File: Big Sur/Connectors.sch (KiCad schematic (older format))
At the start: 11 parts, among them J1 XT30, J10 XT30, J11 XT30, J2 XT30, J3 XT30, J4 XT30, J5 XT30, J6 SMD CASTELLATION PKG, J7 XT30, J8 XT30, J9 XT30

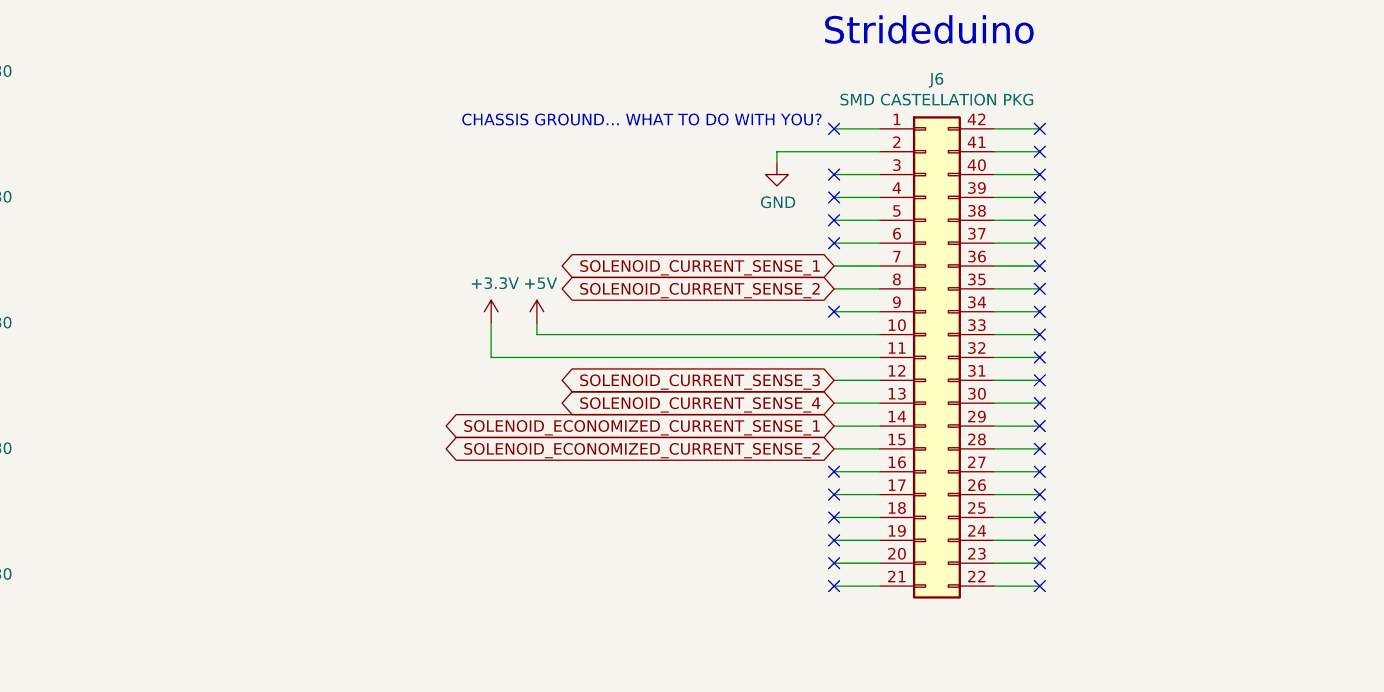
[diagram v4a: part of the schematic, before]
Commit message: Schematics Complete
Still need to spec resistors, and XT30s, then should be ready for layout and routing.
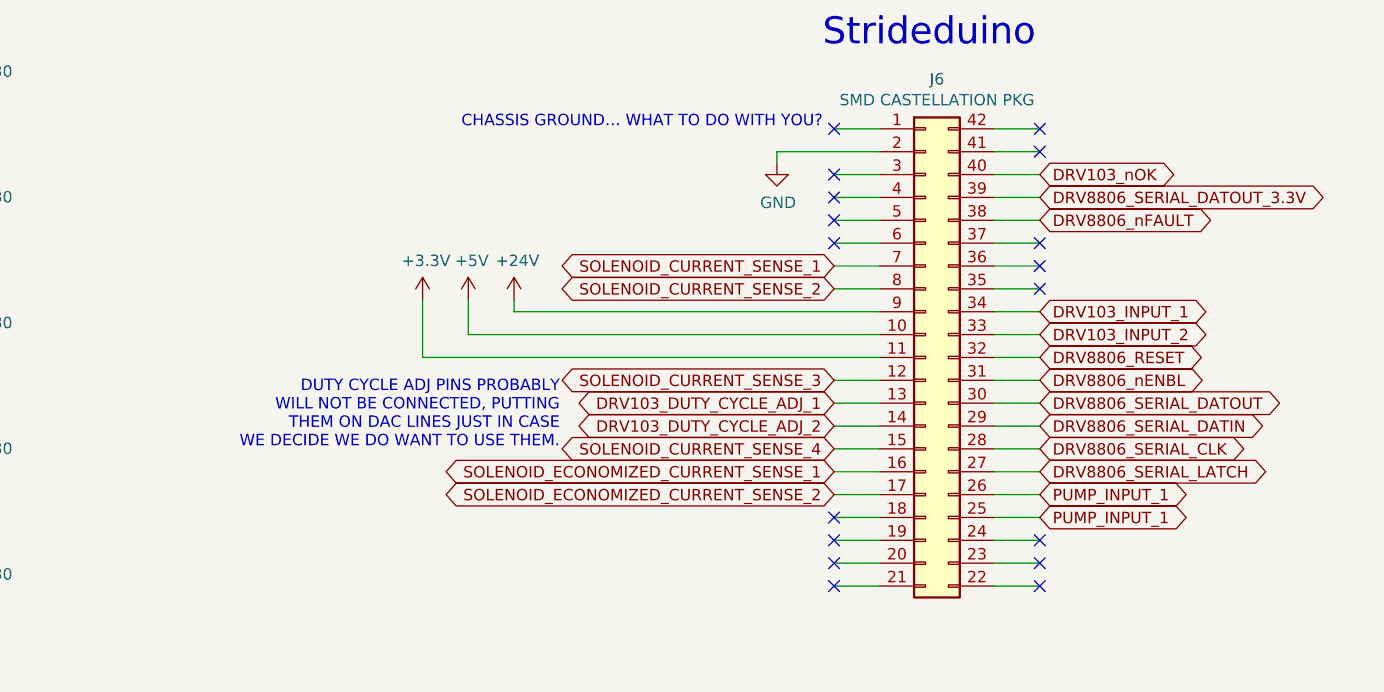
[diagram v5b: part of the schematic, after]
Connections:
- net +24V: now also J6.9 (Pin_9)
- net SOLENOID_CURRENT_SENSE_4: now also J6.15 (Pin_15); no longer J6.13 (Pin_13)
- net SOLENOID_ECONOMIZED_CURRENT_SENSE_1: now also J6.16 (Pin_16); no longer J6.14 (Pin_14)
- net SOLENOID_ECONOMIZED_CURRENT_SENSE_2: now also J6.17 (Pin_17); no longer J6.15 (Pin_15)
- net PUMP_INPUT_1: now reaches J6.25 (Pin_25)
- net PUMP_INPUT_1: now also J6.26 (Pin_26)
- net DRV8806_SERIAL_LATCH: now reaches J6.27 (Pin_27)
- net DRV8806_SERIAL_CLK: now reaches J6.28 (Pin_28)
- net DRV8806_SERIAL_DATIN: now reaches J6.29 (Pin_29)
- net DRV8806_SERIAL_DATOUT: now reaches J6.30 (Pin_30)
- net DRV8806_nENBL: now reaches J6.31 (Pin_31)
- net DRV8806_RESET: now reaches J6.32 (Pin_32)
- net DRV103_INPUT_2: now reaches J6.33 (Pin_33)
- net DRV103_INPUT_1: now reaches J6.34 (Pin_34)
- net DRV8806_nFAULT: now reaches J6.38 (Pin_38)
- net DRV8806_SERIAL_DATOUT_3.3V: now reaches J6.39 (Pin_39)
- net DRV103_nOK: now reaches J6.40 (Pin_40)
- new net DRV103_DUTY_CYCLE_ADJ_1: J6.13 (Pin_13)
- new net DRV103_DUTY_CYCLE_ADJ_2: J6.14 (Pin_14)
- no-connect marks 33 -> 17
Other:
- note added: "DUTY CYCLE ADJ PINS PROBABLY\nWILL NOT BE CONNECTED, PUTTING\nTHEM ON DAC LINES JUST IN CASE\nWE DECIDE WE DO WANT TO USE THEM."
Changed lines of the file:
@@
 NoConn ~ 9650 2150
 NoConn ~ 9650 2250
-NoConn ~ 9650 2350
-NoConn ~ 9650 2450
-NoConn ~ 9650 2550
 NoConn ~ 9650 2650
 NoConn ~ 9650 2750
 NoConn ~ 9650 2850
-NoConn ~ 9650 2950
-NoConn ~ 9650 3050
-NoConn ~ 9650 3150
-NoConn ~ 9650 3250
-NoConn ~ 9650 3350
-NoConn ~ 9650 3450
-NoConn ~ 9650 3550
-NoConn ~ 9650 3650
-NoConn ~ 9650 3750
-NoConn ~ 9650 3850
 NoConn ~ 9650 3950
 NoConn ~ 9650 4050
@@
 NoConn ~ 8750 3950
 NoConn ~ 8750 3850
-NoConn ~ 8750 3750
-NoConn ~ 8750 3650
 NoConn ~ 8750 2650
 NoConn ~ 8750 2550
@@
 L power:+5V #PWR033
 U 1 1 5D8BF1CA
-P 7450 3000
-F 0 "#PWR033" H 7450 2850 50  0001 C CNN
-F 1 "+5V" H 7465 3173 50  0000 C CNN
-F 2 "" H 7450 3000 50  0001 C CNN
-F 3 "" H 7450 3000 50  0001 C CNN
-	1    7450 3000
-	1    0    0    -1
-$EndComp
-Wire Wire Line
-	7450 3000 7450 3050
-Wire Wire Line
-	7450 3050 8950 3050
-Wire Wire Line
-	7250 3000 7250 3150
-Wire Wire Line
-	7250 3150 8950 3150
-Wire Wire Line
-	8750 2950 8950 2950
+P 7150 2900
+F 0 "#PWR033" H 7150 2750 50  0001 C CNN
+F 1 "+5V" H 7165 3073 50  0000 C CNN
+F 2 "" H 7150 2900 50  0001 C CNN
+F 3 "" H 7150 2900 50  0001 C CNN
+	1    7150 2900
+	1    0    0    -1
+$EndComp
+Wire Wire Line
+	7150 2900 7150 3050
+Wire Wire Line
+	7150 3050 8950 3050
+Wire Wire Line
+	6950 2900 6950 3150
+Wire Wire Line
+	6950 3150 8950 3150
 $Comp
 L power:+3.3V #PWR032
 U 1 1 5DA3CFA8
-P 7250 3000
-F 0 "#PWR032" H 7250 2850 50  0001 C CNN
-F 1 "+3.3V" H 7265 3173 50  0000 C CNN
-F 2 "" H 7250 3000 50  0001 C CNN
-F 3 "" H 7250 3000 50  0001 C CNN
-	1    7250 3000
+P 6950 2900
+F 0 "#PWR032" H 6950 2750 50  0001 C CNN
+F 1 "+3.3V" H 6965 3073 50  0000 C CNN
+F 2 "" H 6950 2900 50  0001 C CNN
+F 3 "" H 6950 2900 50  0001 C CNN
+	1    6950 2900
 	1    0    0    -1
 $EndComp
@@
 	4700 3550 4500 3550
 $Comp
-L power:+24V #PWR034
+L power:+24V #PWR035
 U 1 1 5DEE1788
 P 4500 3350
-AR Path="/5D71C3EA/5DEE1788" Ref="#PWR034"  Part="1"
+AR Path="/5D71C3EA/5DEE1788" Ref="#PWR035"  Part="1"
 AR Path="/5D7D29A6/5DEE1788" Ref="#PWR?"  Part="1"
-F 0 "#PWR034" H 4500 3200 50  0001 C CNN
+F 0 "#PWR035" H 4500 3200 50  0001 C CNN
 F 1 "+24V" H 4515 3523 50  0000 C CNN
 F 2 "" H 4500 3350 50  0001 C CNN
@@
 	4700 4100 4500 4100
 $Comp
-L power:+24V #PWR036
+L power:+24V #PWR037
 U 1 1 5DEE50FE
 P 4500 3900
-AR Path="/5D71C3EA/5DEE50FE" Ref="#PWR036"  Part="1"
+AR Path="/5D71C3EA/5DEE50FE" Ref="#PWR037"  Part="1"
 AR Path="/5D7D29A6/5DEE50FE" Ref="#PWR?"  Part="1"
-F 0 "#PWR036" H 4500 3750 50  0001 C CNN
+F 0 "#PWR037" H 4500 3750 50  0001 C CNN
 F 1 "+24V" H 4515 4073 50  0000 C CNN
 F 2 "" H 4500 3900 50  0001 C CNN
@@
 	4700 4650 4500 4650
 $Comp
-L power:+24V #PWR038
+L power:+24V #PWR039
 U 1 1 5DEE5116
 P 4500 4450
-AR Path="/5D71C3EA/5DEE5116" Ref="#PWR038"  Part="1"
+AR Path="/5D71C3EA/5DEE5116" Ref="#PWR039"  Part="1"
 AR Path="/5D7D29A6/5DEE5116" Ref="#PWR?"  Part="1"
-F 0 "#PWR038" H 4500 4300 50  0001 C CNN
+F 0 "#PWR039" H 4500 4300 50  0001 C CNN
 F 1 "+24V" H 4515 4623 50  0000 C CNN
 F 2 "" H 4500 4450 50  0001 C CNN
@@
 	1800 4050 1600 4050
 $Comp
-L power:+24V #PWR035
+L power:+24V #PWR036
 U 1 1 5DEECBB6
 P 1600 3850
-AR Path="/5D71C3EA/5DEECBB6" Ref="#PWR035"  Part="1"
+AR Path="/5D71C3EA/5DEECBB6" Ref="#PWR036"  Part="1"
 AR Path="/5D7D29A6/5DEECBB6" Ref="#PWR?"  Part="1"
-F 0 "#PWR035" H 1600 3700 50  0001 C CNN
+F 0 "#PWR036" H 1600 3700 50  0001 C CNN
 F 1 "+24V" H 1615 4023 50  0000 C CNN
 F 2 "" H 1600 3850 50  0001 C CNN
@@
 	1800 4600 1600 4600
 $Comp
-L power:+24V #PWR037
+L power:+24V #PWR038
 U 1 1 5DEECBCE
 P 1600 4400
-AR Path="/5D71C3EA/5DEECBCE" Ref="#PWR037"  Part="1"
+AR Path="/5D71C3EA/5DEECBCE" Ref="#PWR038"  Part="1"
 AR Path="/5D7D29A6/5DEECBCE" Ref="#PWR?"  Part="1"
-F 0 "#PWR037" H 1600 4250 50  0001 C CNN
+F 0 "#PWR038" H 1600 4250 50  0001 C CNN
 F 1 "+24V" H 1615 4573 50  0000 C CNN
 F 2 "" H 1600 4400 50  0001 C CNN
@@
 Text GLabel 8750 2750 0    50   BiDi ~ 0
 SOLENOID_CURRENT_SENSE_1
-NoConn ~ 8750 2950
 Text GLabel 8750 2850 0    50   BiDi ~ 0
 SOLENOID_CURRENT_SENSE_2
 Text GLabel 8750 3250 0    50   BiDi ~ 0
 SOLENOID_CURRENT_SENSE_3
+Text GLabel 8750 3550 0    50   BiDi ~ 0
+SOLENOID_CURRENT_SENSE_4
+Text GLabel 8750 3650 0    50   BiDi ~ 0
+SOLENOID_ECONOMIZED_CURRENT_SENSE_1
+Text GLabel 8750 3750 0    50   BiDi ~ 0
+SOLENOID_ECONOMIZED_CURRENT_SENSE_2
 Text GLabel 8750 3350 0    50   BiDi ~ 0
-SOLENOID_CURRENT_SENSE_4
+DRV103_DUTY_CYCLE_ADJ_1
 Text GLabel 8750 3450 0    50   BiDi ~ 0
-SOLENOID_ECONOMIZED_CURRENT_SENSE_1
-Text GLabel 8750 3550 0    50   BiDi ~ 0
-SOLENOID_ECONOMIZED_CURRENT_SENSE_2
+DRV103_DUTY_CYCLE_ADJ_2
+Text Notes 7550 3550 2    50   ~ 0
+DUTY CYCLE ADJ PINS PROBABLY\nWILL NOT BE CONNECTED, PUTTING\nTHEM ON DAC LINES JUST IN CASE\nWE DECIDE WE DO WANT TO USE THEM.
+Wire Wire Line
+	7350 2950 7350 2900
+Wire Wire Line
+	7350 2950 8950 2950
+$Comp
+L power:+24V #PWR034
+U 1 1 5D9B6A5F
+P 7350 2900
+F 0 "#PWR034" H 7350 2750 50  0001 C CNN
+F 1 "+24V" H 7365 3073 50  0000 C CNN
+F 2 "" H 7350 2900 50  0001 C CNN
+F 3 "" H 7350 2900 50  0001 C CNN
+	1    7350 2900
+	1    0    0    -1
+$EndComp
+Text GLabel 9650 2350 2    50   BiDi ~ 0
+DRV103_nOK
+Text GLabel 9650 2450 2    50   BiDi ~ 0
+DRV8806_SERIAL_DATOUT_3.3V
+Text GLabel 9650 2550 2    50   BiDi ~ 0
+DRV8806_nFAULT
+Text GLabel 9650 2950 2    50   BiDi ~ 0
+DRV103_INPUT_1
+Text GLabel 9650 3050 2    50   BiDi ~ 0
+DRV103_INPUT_2
+Text GLabel 9650 3650 2    50   BiDi ~ 0
+DRV8806_SERIAL_LATCH
+Text GLabel 9650 3550 2    50   BiDi ~ 0
+DRV8806_SERIAL_CLK
+Text GLabel 9650 3450 2    50   BiDi ~ 0
+DRV8806_SERIAL_DATIN
+Text GLabel 9650 3250 2    50   BiDi ~ 0
+DRV8806_nENBL
+Text GLabel 9650 3150 2    50   BiDi ~ 0
+DRV8806_RESET
+Text GLabel 9650 3350 2    50   BiDi ~ 0
+DRV8806_SERIAL_DATOUT
+Text GLabel 9650 3750 2    50   BiDi ~ 0
+PUMP_INPUT_1
+Text GLabel 9650 3850 2    50   BiDi ~ 0
+PUMP_INPUT_1
 $EndSCHEMATC

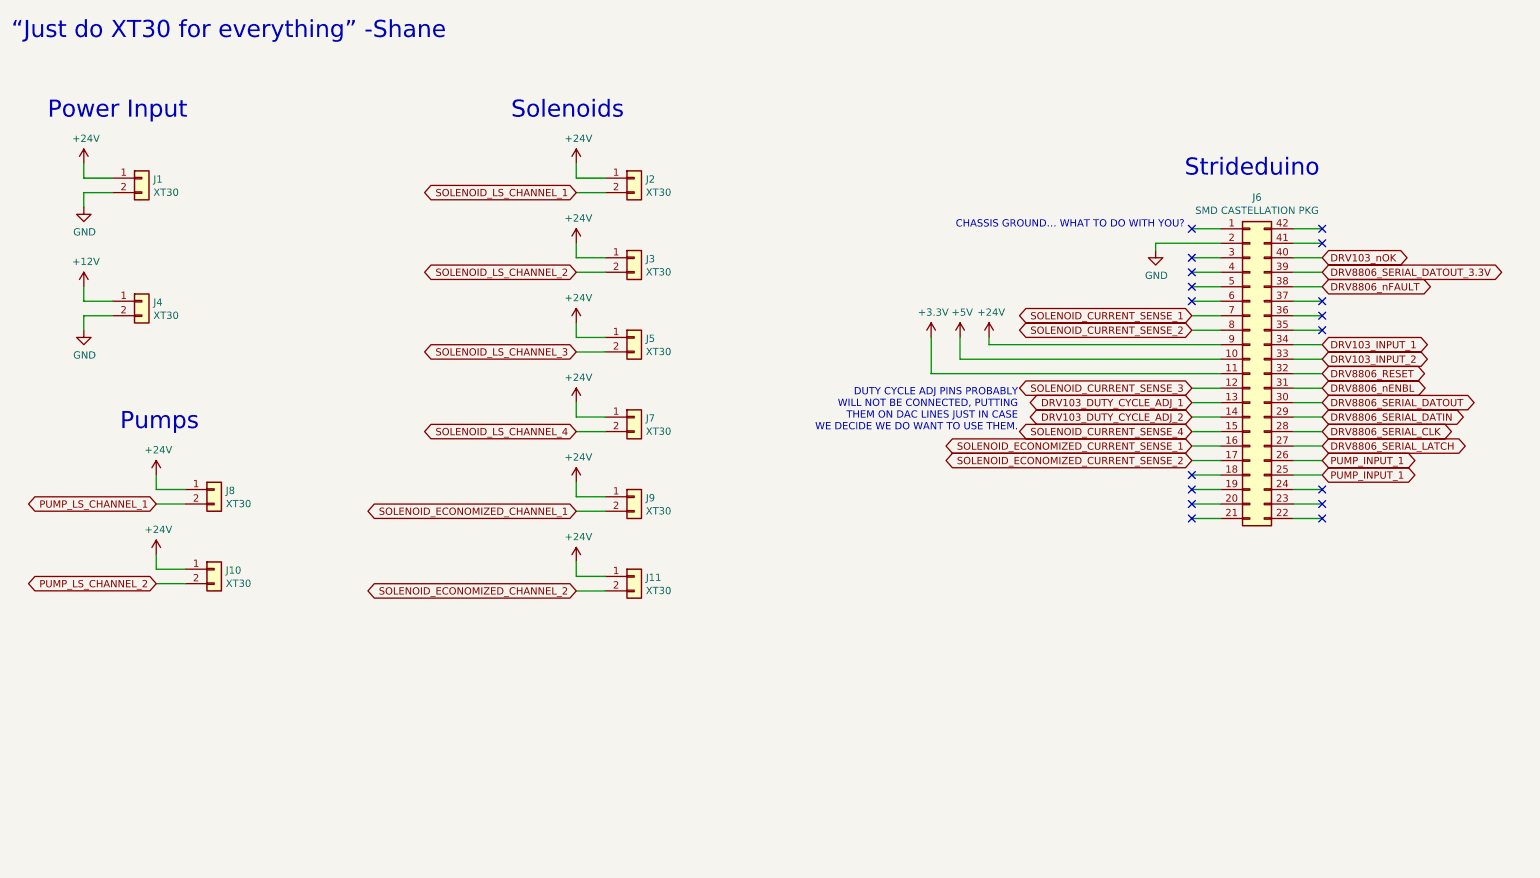
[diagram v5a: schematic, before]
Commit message: Added test points, started CAN connector.
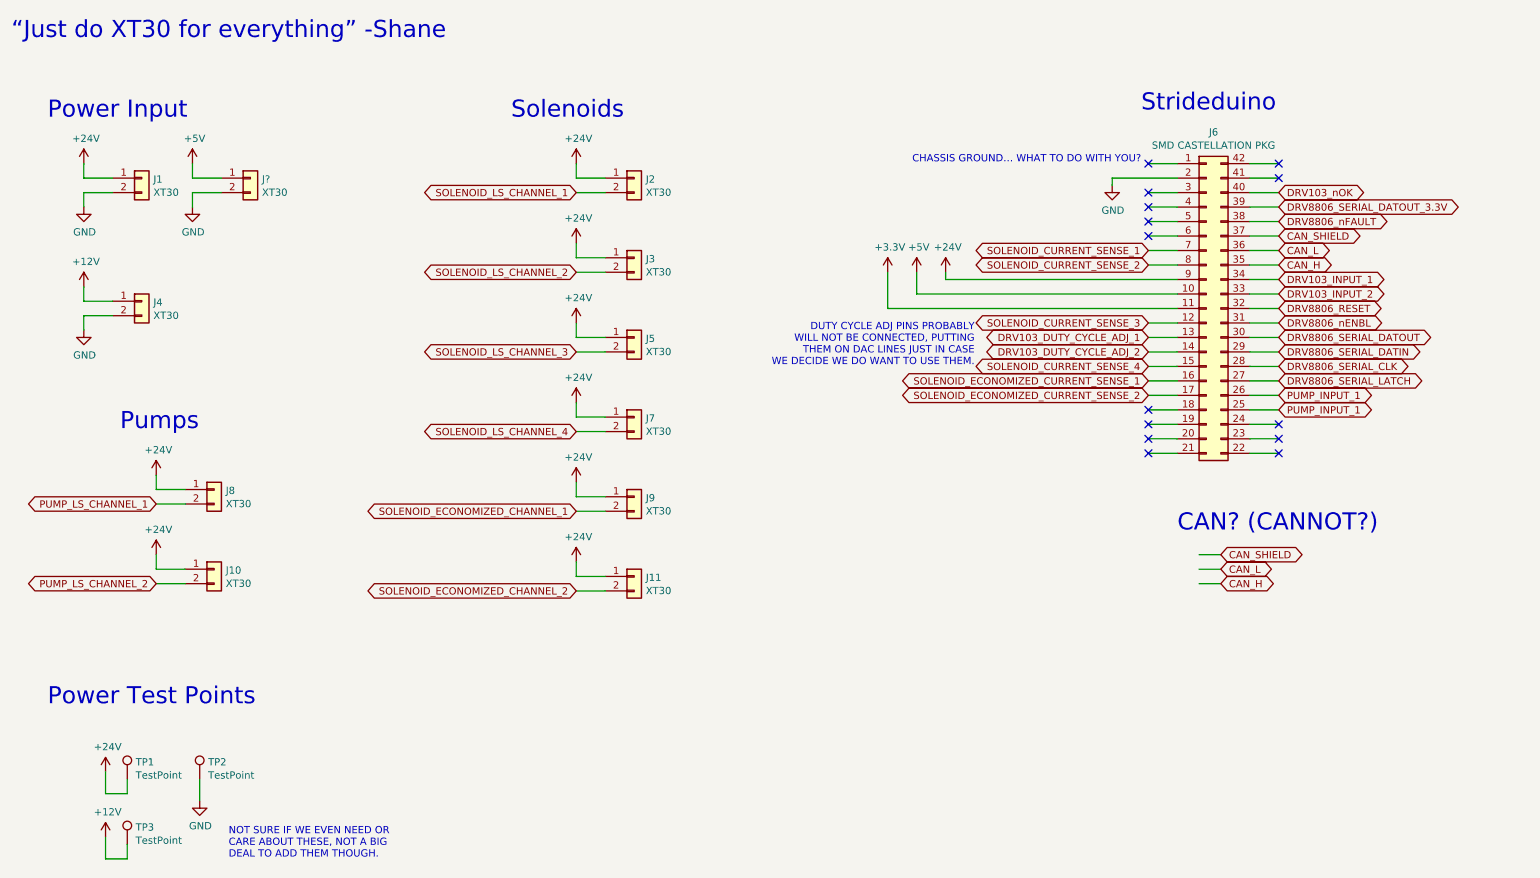
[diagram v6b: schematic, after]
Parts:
- added J?: XT30, symbol Connector_Generic:Conn_01x02
- added TP1, TP2, TP3: TestPoint, symbol Connector:TestPoint
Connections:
- net +12V: now also TP3.1
- net +24V: now also TP1.1
- net +5V: now also J?.1 (Pin_1)
- net GND: now also J?.2 (Pin_2), TP2.1
- net CAN_H: now reaches J6.35 (Pin_35)
- net CAN_L: now reaches J6.36 (Pin_36)
- net CAN_SHIELD: now reaches J6.37 (Pin_37)
- no-connect marks 17 -> 14
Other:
- note added: "CAN? (CANNOT?)"
- note added: "NOT SURE IF WE EVEN NEED OR\nCARE ABOUT THESE, NOT A BIG\nDEAL TO ADD THEM THOUGH."
- note added: "Power Test Points"
- moved on the sheet: J6
